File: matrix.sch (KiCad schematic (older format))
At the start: 153 parts

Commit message: 细节修正
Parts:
- renumbered R4 to RL0
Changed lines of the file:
@@
 EESchema Schematic File Version 4
 LIBS:keyboard-cache
-LIBS:ble4100-nrf-cache
 EELAYER 26 0
 EELAYER END
@@
 col14
 $Comp
-L device1:R R4
+L device1:R RL0
 U 1 1 5043A0D0
 P 14550 3000
-F 0 "R4" V 14630 3000 50  0000 C CNN
+F 0 "RL0" V 14630 3000 50  0000 C CNN
 F 1 "300" V 14550 3000 50  0000 C CNN
 F 2 "Resistor_SMD:R_0805_2012Metric" H 14550 3000 60  0001 C CNN

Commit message: 修正几个问题
修正ADC接口不正确的问题
增加防反冲二极管
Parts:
- renumbered S031 to S3001, S041 to S4001
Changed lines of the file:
@@
 $EndComp
 $Comp
-L mx1a-simple:MX1A S041
+L mx1a-simple:MX1A S4001
 U 1 1 50410564
 P 3350 7350
-F 0 "S041" H 3200 7600 60  0000 C CNN
+F 0 "S4001" H 3200 7600 60  0000 C CNN
 F 1 "MX1A" H 3350 7450 60  0000 C CNN
 F 2 "MX1A:MX1A-simple" H 3350 7350 60  0001 C CNN
@@
 col8
 $Comp
-L mx1a-simple:MX1A S031
+L mx1a-simple:MX1A S3001
 U 1 1 5042A9E4
 P 3300 5450
-F 0 "S031" H 3150 5700 60  0000 C CNN
+F 0 "S3001" H 3150 5700 60  0000 C CNN
 F 1 "MX1A" H 3300 5550 60  0000 C CNN
 F 2 "MX1A:MX1A-simple" H 3300 5450 60  0001 C CNN

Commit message: 替换接口为Type-C
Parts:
- D1, D10, D11, D12, D13, D14, D15, D16, D17, D18, D19, D2, D21, D22, D23, D24, D26, D27, D28, D29, D3, D30, D31, D32, D33, D34, D36, D37, D38, D39, D4, D41, D42, D43, D44, D46, D47, D48, D49, D5, D50, D51, D52, D53, D54, D55, D56, D57, D58, D59, D6, D60, D61, D62, D63, D64, D65, D66, D67, D68, D69, D7, D70, D8, D9: symbol device1:DIODE -> keyboard-rescue:DIODE-device1
- DC1, DC2, DC3: symbol device1:LED -> keyboard-rescue:LED-device1
- RL0: symbol device1:R -> keyboard-rescue:R-device1
- S1, S10, S101, S102, S11, S12, S13, S14, S15, S151, S16, S17, S18, S19, S2, S21, S22, S23, S24, S26, S27, S28, S29, S3, S30, S3001, S301, S302, S31, S32, S33, S34, S36, S37, S38, S39, S4, S4001, S41, S42, S43, S44, S46, S47, S48, S49, S5, S50, S51, S512, S52, S53, S54, S55, S552, S56, S57, S58, S59, S6, S60, S601, S602, S61, S62, S63, S64, S641, S65, S6512, S66, S661, S67, S68, S681, S682, S69, S691, S692, S7, S70, S7012, S8, S9: symbol mx1a-simple:MX1A -> keyboard-rescue:MX1A-mx1a-simple

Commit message: 添加一些文字说明
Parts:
- D1, D10, D11, D12, D13, D14, D15, D16, D17, D18, D19, D2, D21, D22, D23, D24, D26, D27, D28, D29, D3, D30, D31, D32, D33, D34, D36, D37, D38, D39, D4, D41, D42, D43, D44, D46, D47, D48, D49, D5, D50, D51, D52, D53, D54, D55, D56, D57, D58, D59, D6, D60, D61, D62, D63, D64, D65, D66, D67, D68, D69, D7, D70, D8, D9: symbol keyboard-rescue:DIODE-device1 -> device1:DIODE
- D100: renamed from DC1; symbol keyboard-rescue:LED-device1 -> device1:LED
- D1001: renamed from DC2; symbol keyboard-rescue:LED-device1 -> device1:LED
- D1002: renamed from DC3; symbol keyboard-rescue:LED-device1 -> device1:LED
- R100: renamed from RL0; symbol keyboard-rescue:R-device1 -> device1:R

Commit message: 修正阵列二极管在原理图上的方向与封装方向不一致的问题
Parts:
- D1, D10, D11, D12, D13, D14, D15, D16, D17, D18, D19, D2, D21, D22, D23, D24, D26, D27, D28, D29, D3, D30, D31, D32, D33, D34, D36, D37, D38, D39, D4, D41, D42, D43, D44, D46, D47, D48, D49, D5, D50, D51, D52, D53, D54, D55, D56, D57, D58, D59, D6, D60, D61, D62, D63, D64, D65, D66, D67, D68, D69, D7, D70, D8, D9: symbol device1:DIODE -> Diode:1N4148
- D100, D1001, D1002: symbol device1:LED -> Device:LED
- R100: symbol device1:R -> Device:R
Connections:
- wire segments 423 -> 559

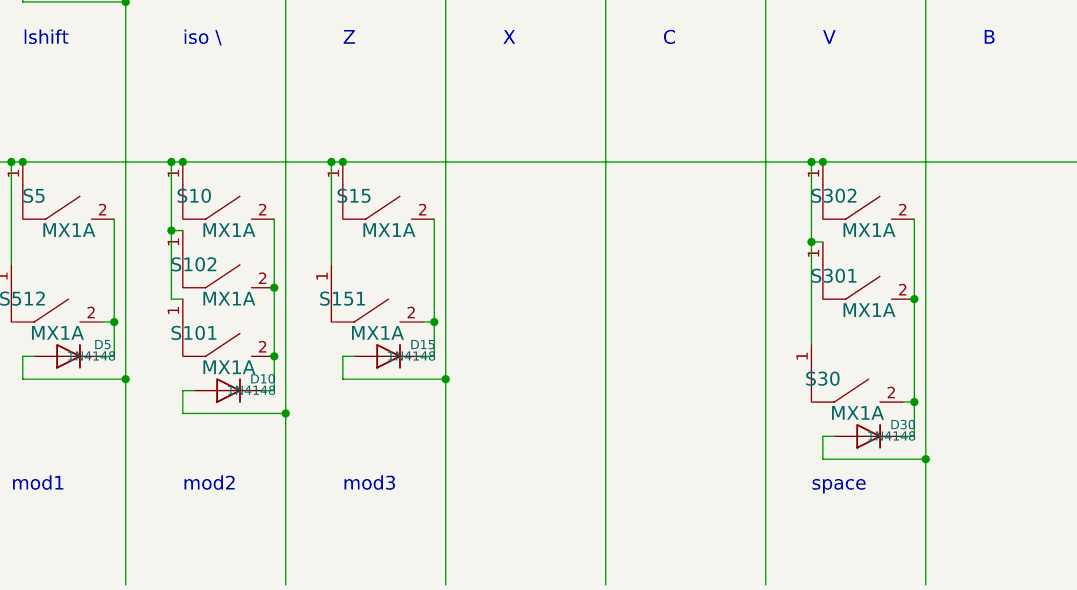
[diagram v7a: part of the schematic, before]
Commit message: 改进了空格和左GUI键的接线顺序，使其更难粘连
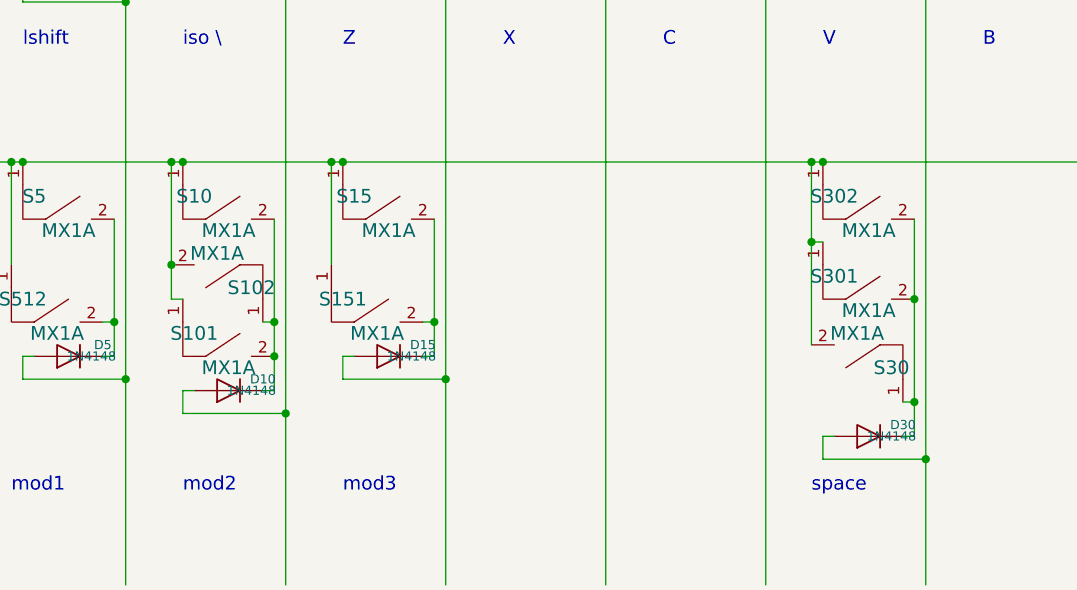
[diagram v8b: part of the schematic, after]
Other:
- moved on the sheet: S102, S30
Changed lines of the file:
@@
-$EndComp
-$Comp
-L keyboard-rescue:MX1A-mx1a-simple S102
-U 1 1 5040EEA3
-P 4050 8850
-F 0 "S102" H 3900 9100 60  0000 C CNN
-F 1 "MX1A" H 4050 8950 60  0000 C CNN
-F 2 "MX1A:MX1A-simple" H 4050 8850 60  0001 C CNN
-F 3 "" H 4050 8850 60  0001 C CNN
-	1    4050 8850
-	1    0    0    -1
 $EndComp
 $Comp
@@
 L keyboard-rescue:MX1A-mx1a-simple S30
 U 1 1 5040DF35
-P 6800 9350
-F 0 "S30" H 6650 9600 60  0000 C CNN
-F 1 "MX1A" H 6800 9450 60  0000 C CNN
-F 2 "MX1A:MX1A-simple" H 6800 9350 60  0001 C CNN
-F 3 "" H 6800 9350 60  0001 C CNN
-	1    6800 9350
-	1    0    0    -1
+P 6800 8800
+F 0 "S30" H 6650 9050 60  0000 C CNN
+F 1 "MX1A" H 6800 8900 60  0000 C CNN
+F 2 "MX1A:MX1A-simple" H 6800 8800 60  0001 C CNN
+F 3 "" H 6800 8800 60  0001 C CNN
+	1    6800 8800
+	-1   0    0    1
 $EndComp
 Text Notes 8700 2450 0    120  ~ 0
@@
 	3800 8750 3850 8750
 Connection ~ 3800 8150
-Wire Wire Line
-	3800 8150 3800 8450
 Connection ~ 4500 8150
 Wire Wire Line
@@
 	11950 8400 11950 8850
 Connection ~ 11250 8700
-Wire Wire Line
-	4250 8400 4250 8700
 Wire Wire Line
 	1800 5150 3100 5150
@@
 Wire Wire Line
 	3850 9150 3850 9250
-Wire Wire Line
-	3850 9250 4300 9250
 Wire Wire Line
 	4550 9100 5000 9100
@@
 Connection ~ 9450 8150
 Connection ~ 12650 3500
-Wire Wire Line
-	3850 8450 3800 8450
-Connection ~ 3800 8450
-Connection ~ 4250 8700
 Connection ~ 7050 8750
 Wire Wire Line
@@
 Wire Wire Line
 	12650 3500 12650 3700
-Wire Wire Line
-	3800 8450 3800 8750
-Wire Wire Line
-	4250 8700 4250 9000
 Wire Wire Line
 	7050 8750 7050 9200
@@
 Wire Wire Line
 	12600 9000 12650 9000
+Wire Wire Line
+	4250 8400 4250 8850
+Wire Wire Line
+	3850 9250 4300 9250
+$Comp
+L keyboard-rescue:MX1A-mx1a-simple S102
+U 1 1 5040EEA3
+P 4000 8450
+F 0 "S102" H 3850 8700 60  0000 C CNN
+F 1 "MX1A" H 4000 8550 60  0000 C CNN
+F 2 "MX1A:MX1A-simple" H 4000 8450 60  0001 C CNN
+F 3 "" H 4000 8450 60  0001 C CNN
+	1    4000 8450
+	-1   0    0    1
+$EndComp
+Connection ~ 3800 8600
+Wire Wire Line
+	3800 8600 3800 8750
+Wire Wire Line
+	3800 8150 3800 8600
+Wire Wire Line
+	4200 8850 4250 8850
+Connection ~ 4250 8850
+Wire Wire Line
+	4250 8850 4250 9000
 $EndSCHEMATC
